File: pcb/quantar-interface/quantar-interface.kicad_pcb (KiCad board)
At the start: 4 copper layers, 127 x 101.6 mm, 179 parts, among them J1 DC Input, J2 USB_A, J3 USB_B, J4 GPIO, J5 Quantar Audio, J6 Ext. Alarm Contact, J7 Ext. TX Inhb., J8 Quantar, J9 5V Out, K1 G6S-2, Q1 DMP3056L-7, Q2 2N7002, Q3 2N7002, Q4 2N7002, Q5 2N7002, Q6 2N7002, SW1 SW_TX_INHB, SW2 SW_PTT_INHB, T1 Transformer, T2 Transformer, U1 M93C46, U10 4N27, U11 4N27, U12 4N27, U13 4N27, U14 4N27, U15 74HC14, U2 LM386, U3 TPS562200, U4 AP1506, U5 CM119A, U6 LM1117-5.0, U7 LM555, U8 4N27, U9 4N27, Y1 12MHz

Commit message: Add fiducials for PCBA
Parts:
- added REF1: Fiducial_1mm_Mask2mm, Fiducial:Fiducial_1mm_Mask2mm, F.Cu at (189.2, 62.2)
- added REF2: Fiducial_1mm_Mask2mm, Fiducial:Fiducial_1mm_Mask2mm, F.Cu at (81.3, 142.2)
- moved C15 76.2 mm to (168.1, 130.6)
- moved C17 76.2 mm to (134.1, 128.8)
- moved C25 76.2 mm to (134.1, 122.2)
- moved C27 76.2 mm to (117.9, 127.7)
- moved C32 76.2 mm to (107.5, 144.0)
- moved C33 76.2 mm to (119.4, 138.9)
- moved C7 76.2 mm to (150.4, 141.5)
- moved D10 76.2 mm to (140.5, 128.0)
- moved D13 76.2 mm to (134.9, 75.9)
- moved D19 76.2 mm to (130.3, 111.5)
- moved J7 76.2 mm to (153.7, 59.7)
- moved J9 76.2 mm to (99.7, 122.4)
- moved Q3 76.2 mm to (134.9, 80.3)
- moved R1 76.2 mm to (86.9, 124.2)
- moved R11 76.2 mm to (103.9, 105.4)
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
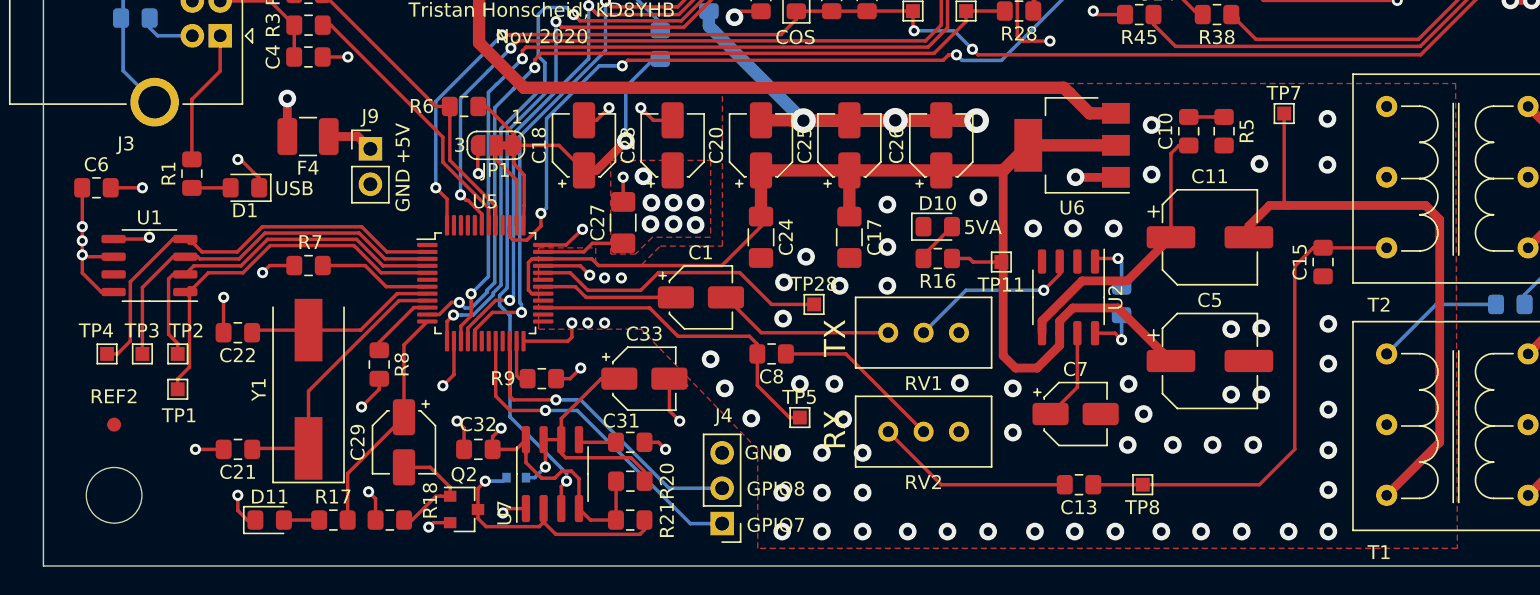
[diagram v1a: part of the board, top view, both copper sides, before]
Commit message: Add bottom layer plane to analog area
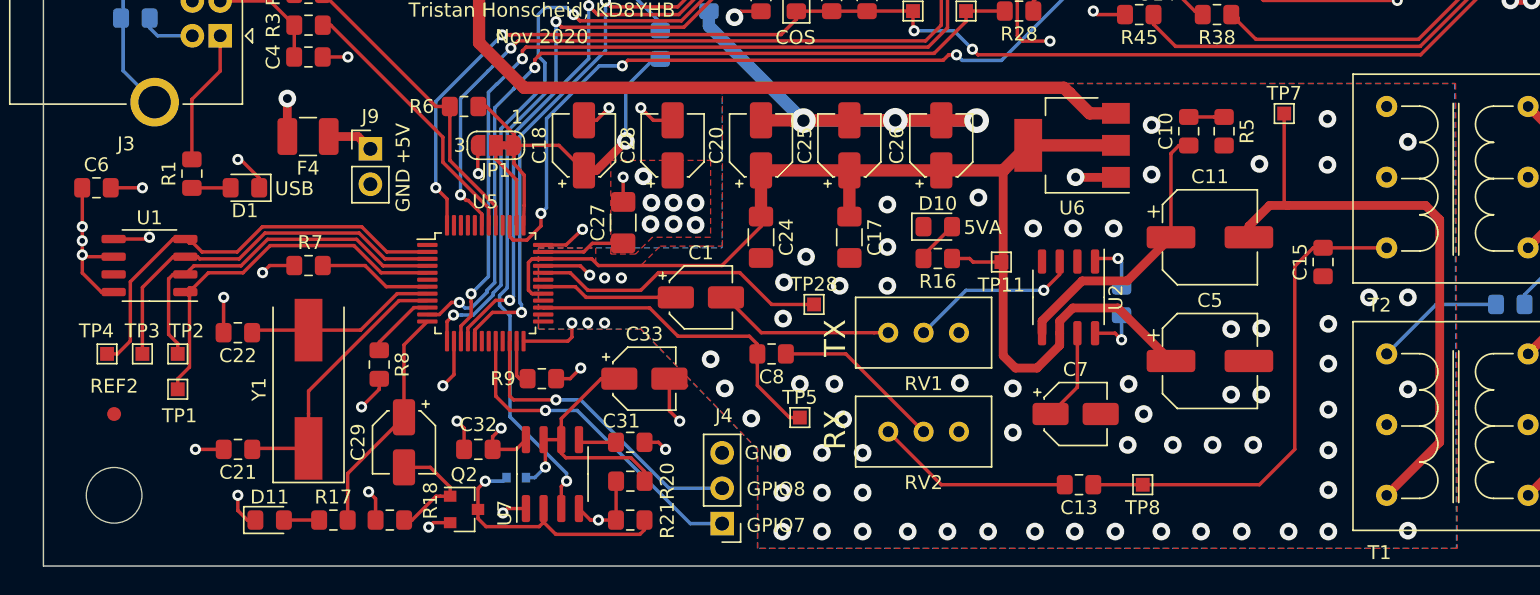
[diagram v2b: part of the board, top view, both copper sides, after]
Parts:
- moved REF2 0.76 mm to (81.3, 141.5)
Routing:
- net +5V: track 44.1 -> 35.6 mm, vias 23 -> 24
- net GNDA: vias 69 -> 74
- added copper zone on B.Cu, net GNDA
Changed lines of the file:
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@@
     (35 F.Paste user hide)
     (36 B.SilkS user)
-    (37 F.SilkS user)
+    (37 F.SilkS user hide)
     (38 B.Mask user)
-    (39 F.Mask user)
+    (39 F.Mask user hide)
     (40 Dwgs.User user)
     (41 Cmts.User user hide)
@@
     (43 Eco2.User user hide)
     (44 Edge.Cuts user)
-    (45 Margin user hide)
-    (46 B.CrtYd user hide)
-    (47 F.CrtYd user hide)
+    (45 Margin user)
+    (46 B.CrtYd user)
+    (47 F.CrtYd user)
     (48 B.Fab user hide)
     (49 F.Fab user hide)
@@
   )
   (module Fiducial:Fiducial_1mm_Mask2mm (layer F.Cu)
-    (at 81.28 142.24)
+    (at 81.28 141.478)
     (descr "Circular Fiducial, 1mm bare copper, 2mm soldermask opening (Level A)")
     (tags fiducial)
@@
   (segment (start 98.062 149.098) (end 98.062 145.756) (width 0.25) (layer F.Cu) (net 26))
   (segment (start 115.508 149.098) (end 114.681 148.271) (width 0.25) (layer F.Cu) (net 3))
-  (segment (start 117.339 149.098) (end 115.508 149.098) (width 0.25) (layer F.Cu) (net 3))
+  (segment (start 117.339 149.098) (end 116.078 149.098) (width 0.25) (layer F.Cu) (net 3))
   (segment (start 117.348 149.089) (end 117.339 149.098) (width 0.25) (layer F.Cu) (net 3))
   (segment (start 117.348 146.304) (end 117.348 149.089) (width 0.25) (layer F.Cu) (net 3))
-  (segment (start 114.681 148.271) (end 114.681 146.119998) (width 0.25) (layer F.Cu) (net 3))
-  (segment (start 114.681 146.119998) (end 114.140001 145.578999) (width 0.25) (layer F.Cu) (net 3))
-  (segment (start 113.443999 145.578999) (end 112.935999 146.086999) (width 0.25) (layer F.Cu) (net 3))
-  (segment (start 114.140001 145.578999) (end 113.443999 145.578999) (width 0.25) (layer F.Cu) (net 3))
-  (segment (start 110.871 144.296) (end 110.871 143.321) (width 0.25) (layer F.Cu) (net 3))
-  (segment (start 112.935999 146.086999) (end 111.993997 146.086999) (width 0.25) (layer F.Cu) (net 3))
-  (segment (start 111.993997 146.086999) (end 110.871 144.964002) (width 0.25) (layer F.Cu) (net 3))
-  (segment (start 110.871 144.964002) (end 110.871 144.296) (width 0.25) (layer F.Cu) (net 3))
   (via (at 86.614 86.6775) (size 1.778) (drill 0.889) (layers F.Cu B.Cu) (net 3))
   (via (at 86.6775 91.694) (size 1.778) (drill 0.889) (layers F.Cu B.Cu) (net 3))
@@
   (via (at 93.726 118.8085) (size 1.27) (drill 0.635) (layers F.Cu B.Cu) (net 3))
   (segment (start 93.726 121.539) (end 93.726 118.8085) (width 0.635) (layer F.Cu) (net 3))
+  (segment (start 115.824 149.098) (end 115.508 149.098) (width 0.25) (layer F.Cu) (net 3))
+  (segment (start 116.078 149.098) (end 115.824 149.098) (width 0.25) (layer F.Cu) (net 3))
+  (via (at 116.078 149.098) (size 0.8) (drill 0.4) (layers F.Cu B.Cu) (net 3))
   (segment (start 83.829 113.73) (end 83.829 113.03) (width 0.25) (layer B.Cu) (net 4))
   (segment (start 84.399 114.3) (end 83.829 113.73) (width 0.25) (layer B.Cu) (net 4))
@@
   (via (at 155.829 124.2695) (size 1.27) (drill 0.635) (layers F.Cu B.Cu) (net 8))
   (via (at 155.829 120.7135) (size 1.27) (drill 0.635) (layers F.Cu B.Cu) (net 8))
+  (via (at 171.45 133.096) (size 1.27) (drill 0.635) (layers F.Cu B.Cu) (net 8))
+  (via (at 174.244 133.096) (size 1.27) (drill 0.635) (layers F.Cu B.Cu) (net 8))
+  (via (at 174.244 139.7) (size 1.27) (drill 0.635) (layers F.Cu B.Cu) (net 8))
+  (via (at 174.244 149.86) (size 1.27) (drill 0.635) (layers F.Cu B.Cu) (net 8))
+  (via (at 174.244 121.92) (size 1.27) (drill 0.635) (layers F.Cu B.Cu) (net 8))
   (segment (start 150.495 139.551) (end 148.568 141.478) (width 0.25) (layer F.Cu) (net 9))
   (segment (start 150.495 135.671) (end 150.495 139.551) (width 0.25) (layer F.Cu) (net 9))
@@
       )
     )
+  )
+  (zone (net 8) (net_name GNDA) (layer B.Cu) (hatch edge 0.508)
+    (connect_pads yes (clearance 0.508))
+    (min_thickness 0.254)
+    (fill yes (arc_segments 32) (thermal_gap 0.508) (thermal_bridge_width 0.508))
+    (polygon
+      (pts
+        (xy 177.7365 151.13) (xy 127.508 151.13) (xy 127.508 144.018) (xy 119.126 135.382) (xy 111.76 135.382)
+        (xy 111.76 129.54) (xy 124.968 129.54) (xy 124.968 117.729) (xy 177.6095 117.729)
+      )
+    )

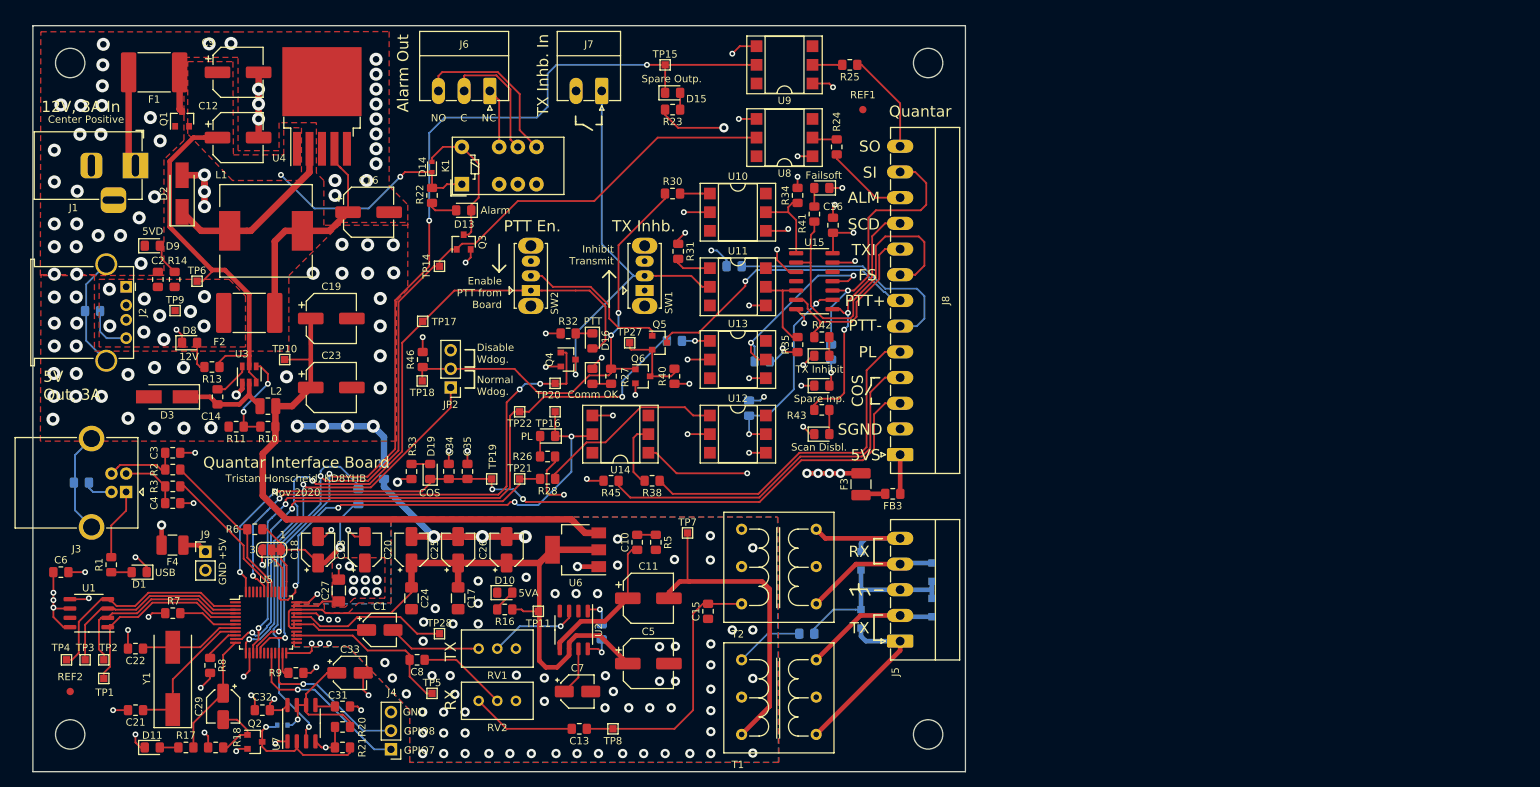
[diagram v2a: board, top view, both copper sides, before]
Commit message: Merge split ground planes, connect mounting holes to GND
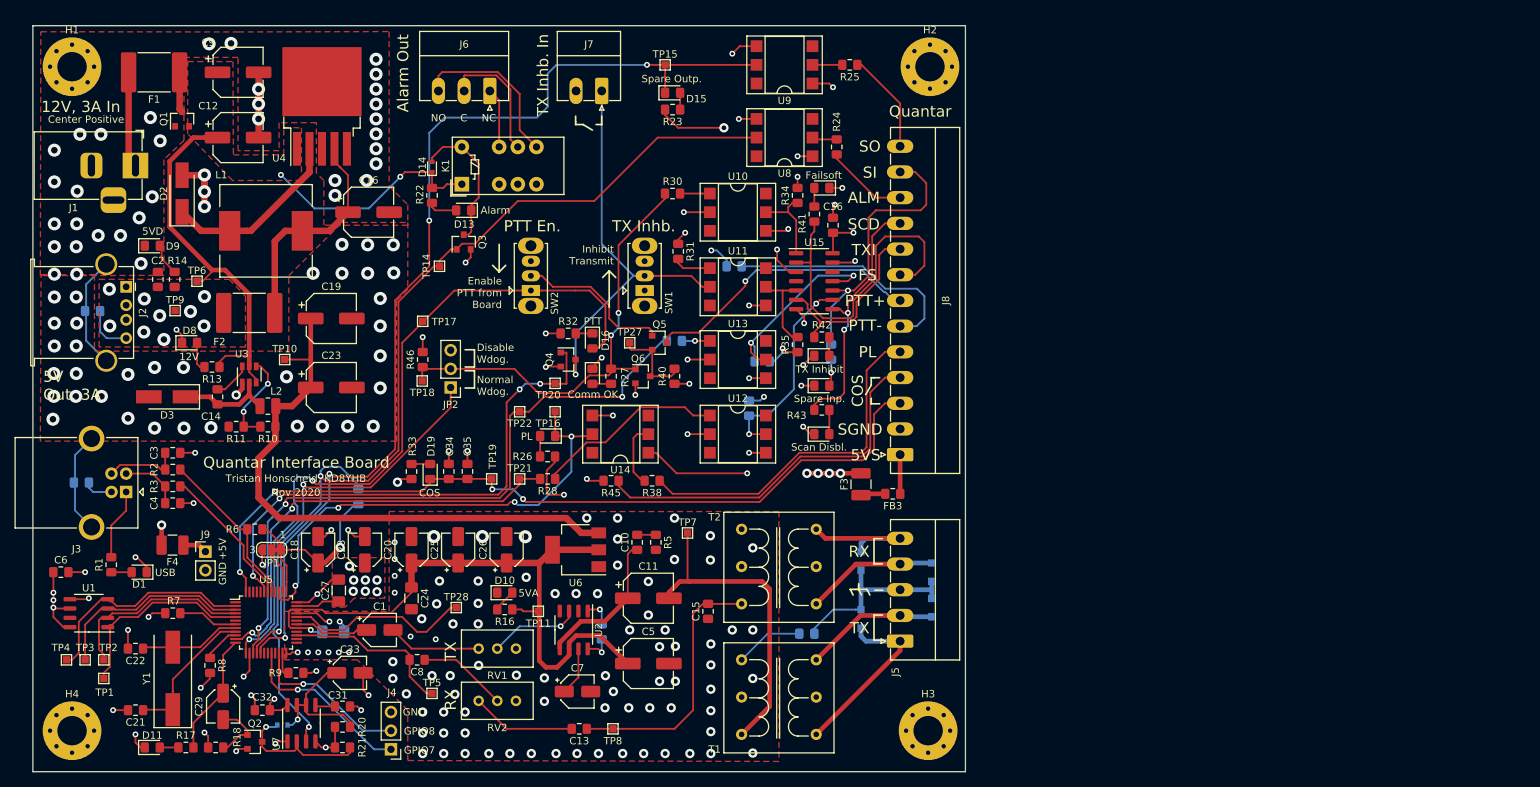
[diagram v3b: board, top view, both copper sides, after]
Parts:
- removed R15: 0, Resistor_SMD:R_0805_2012Metric_Pad1.15x1.40mm_HandSolder
- removed REF1, REF2: Fiducial_1mm_Mask2mm, Fiducial:Fiducial_1mm_Mask2mm
- C17: moved to B.Cu
- H1, H2, H3, H4: value MountingHole -> MountingHole_Pad; footprint MountingHole:MountingHole_4mm -> MountingHole:MountingHole_4mm_Pad_Via
- moved C17 17.6 mm to (117.1, 133.3), turned to 0 degrees
- moved TP28 4.23 mm to (133.9, 130.0)
- moved H1 0.57 mm to (81.5, 56.4)
- moved H2 0.57 mm to (198.4, 56.4)
- moved H4 0.57 mm to (81.5, 146.8)
- moved H3 0.51 mm to (198.1, 146.8)
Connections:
- C15 pad 2: GNDA -> GND
- C17 pad 2: GNDA -> GND
- C20 pad 2: GNDA -> GND
- C24 pad 2: GNDA -> GND
- C25 pad 2: GNDA -> GND
- C26 pad 2: GNDA -> GND
- C5 pad 2: GNDA -> Net-(C5-Pad2)
- C7 pad 2: GNDA -> Net-(C7-Pad2)
- D10 pad 1: GNDA -> GND
- H1 pad 1: (no net) -> GND
- H2 pad 1: (no net) -> GND
- H3 pad 1: (no net) -> GND
- H4 pad 1: (no net) -> GND
- R12 pad 2: GNDA -> GND
- R5 pad 2: GNDA -> GND
- RV1 pad 3: GNDA -> GND
- RV2 pad 3: GNDA -> GND
- T1 pad 1: GNDA -> GND
- T2 pad 1: GNDA -> GND
- U2 pad 2: GNDA -> GND
- U2 pad 4: GNDA -> GND
- U5 pad 24: GNDA -> GND
- U5 pad 33: GNDA -> GND
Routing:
- net GNDA: track 56.2 -> 0.00 mm, vias 74 -> 0
- net GND: track 153.3 -> 165.9 mm, vias 120 -> 202
- net /LINEOUT_RIGHT: track 21.5 -> 25.4 mm
- net Net-(C19-Pad1): track 79.6 -> 80.6 mm
- net +5VA: track 88.7 -> 89.1 mm, vias 0 -> 1
- removed copper zone on B.Cu, net GNDA
- removed copper zone on F.Cu, net GNDA
- removed copper zone on In2.Cu, net GNDA

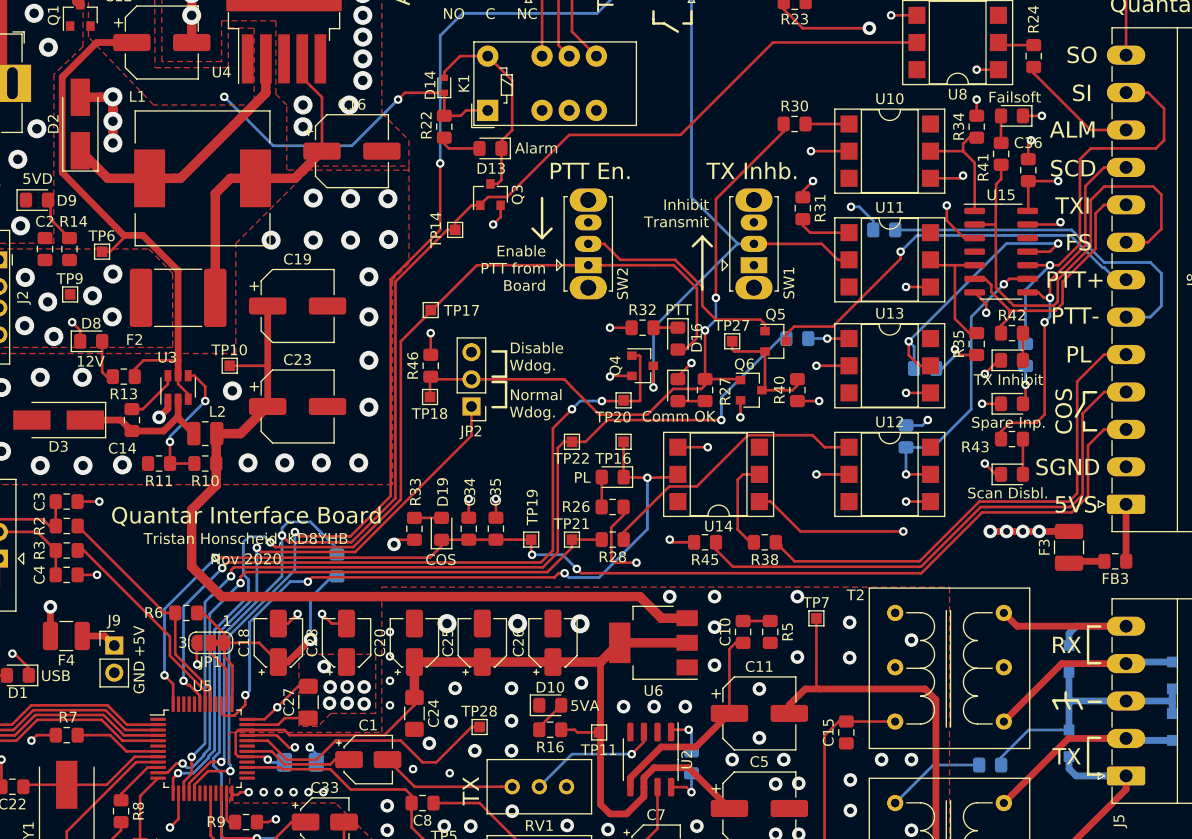
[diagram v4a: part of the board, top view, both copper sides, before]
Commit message: Plot gerbers, generate JLCPCB BOM and picklist, move all JLC components to top side
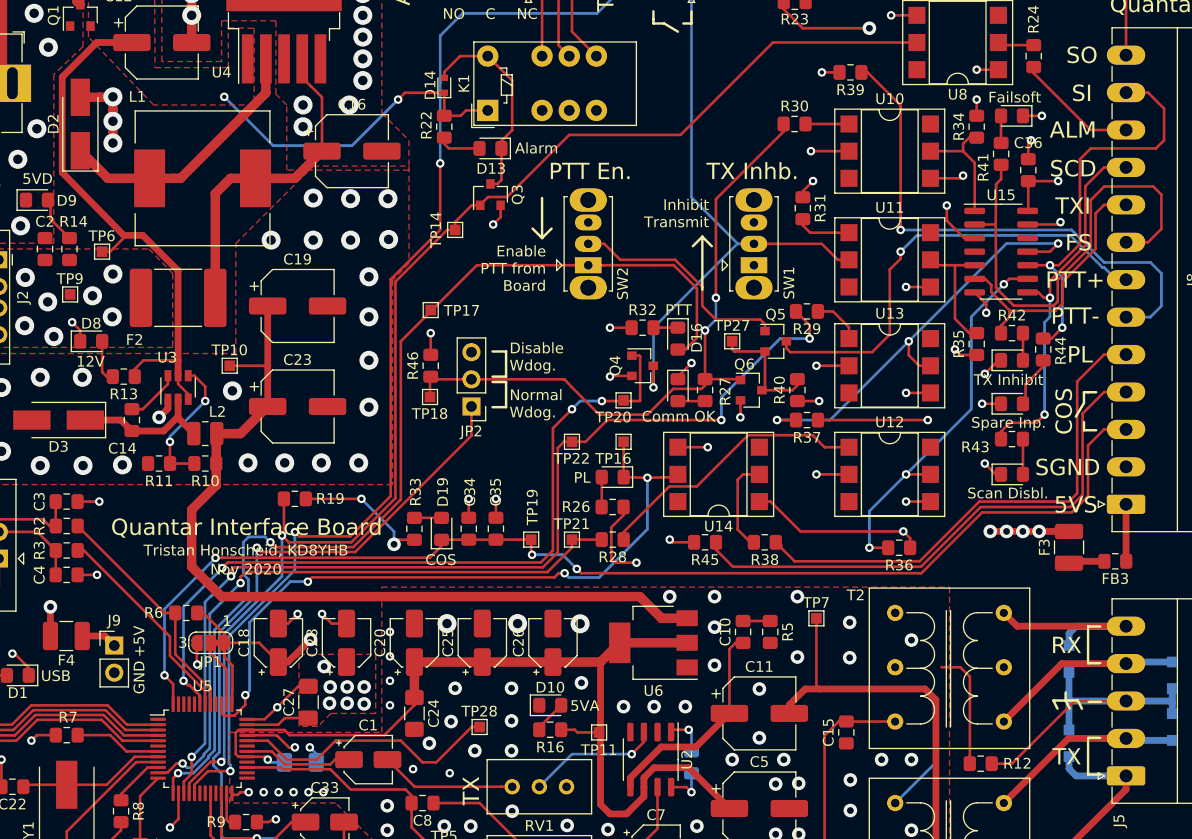
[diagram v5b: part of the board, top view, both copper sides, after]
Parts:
- R12, R19, R29, R36, R37, R39, R44: moved to F.Cu
- moved R39 15.1 mm to (168.5, 68.8)
- moved R37 12.0 mm to (164.5, 101.3)
- moved R36 10.4 mm to (173.1, 113.3), turned to 180 degrees
- moved R19 7.36 mm to (116.6, 108.7), turned to 180 degrees
- moved R29 2.69 mm to (164.5, 91.2)
- moved R44 1.73 mm to (186.6, 94.7)
- moved R12 0.89 mm to (180.7, 133.5)
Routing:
- net /STATION_PTT_LED+: track 33.4 -> 49.4 mm, vias 0 -> 1
- net Net-(R37-Pad2): track 27.4 -> 41.8 mm, vias 2 -> 3
- net Net-(R36-Pad2): track 27.8 -> 36.3 mm, vias 2 -> 3
- net /STATION_5V: track 41.5 -> 48.4 mm
- net Net-(D4-Pad2): track 25.5 -> 32.4 mm
- net GND: track 165.9 -> 172.7 mm
- net /SPARE_INPUT: track 90.6 -> 95.8 mm, vias 3 -> 4
- net /STATION_PTT_LED-: track 38.4 -> 42.8 mm
- net /ALARM: track 127.3 -> 123.1 mm
- net +5V: track 35.6 -> 33.8 mm
- net +3V3: track 159.9 -> 161.2 mm, vias 4 -> 5
- net Net-(D23-Pad2): track 3.65 -> 4.84 mm, vias 1 -> 0
- net Net-(R29-Pad1): track 3.81 -> 4.58 mm, vias 1 -> 0
- net /STATION_SPARE_INPUT: track 37.7 -> 37.9 mm, vias 1 -> 2

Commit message: Revision B
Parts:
- added R15: 100K, Resistor_SMD:R_0805_2012Metric_Pad1.15x1.40mm_HandSolder, F.Cu at (151.4, 88.5)
- added SW3: Force PTT, Button_Switch_SMD:SW_Push_1P1T_NO_CK_KMR2, F.Cu at (156.1, 70.1)
- moved C6 8.62 mm to (78.6, 133.7), turned to 270 degrees
- moved F4 1.23 mm to (94.0, 121.5)
- moved J5 0.76 mm to (195.1, 134.6)
- moved J6 0.76 mm to (138.4, 58.9)
- moved J7 0.76 mm to (153.7, 58.9)
- moved J8 0.76 mm to (195.1, 109.2)
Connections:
- C5 pad 2: Net-(C5-Pad2) -> GND
- C7 pad 2: Net-(C7-Pad2) -> GND
- D16 pad 1: Net-(D16-Pad1) -> /STATION_PTT_LED-
- D16 pad 2: /PTT -> Net-(D16-Pad2)
- R32 pad 1: GND -> +5V
- R32 pad 2: Net-(D16-Pad1) -> Net-(D16-Pad2)
- SW2 pad 3: GND -> Net-(SW2-Pad3)
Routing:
- net /STATION_PTT_LED-: track 42.8 -> 83.6 mm, vias 1 -> 3
- net /PTT: track 97.8 -> 79.9 mm
- net GND: track 172.7 -> 177.7 mm, vias 202 -> 204
- net /ALARM: track 123.1 -> 127.5 mm
- net Net-(D16-Pad2): track 0.00 -> 3.39 mm
- net Net-(J6-Pad2): track 17.4 -> 20.4 mm
- net Net-(D16-Pad1): track 2.29 -> 0.00 mm
- net Net-(J6-Pad3): track 22.7 -> 25.0 mm
- net /STATION_PTT_LED+: track 49.4 -> 51.3 mm
- net /STATION_SPARE_INPUT: track 37.9 -> 39.6 mm
- net /STATION_FAILSOFT: track 45.5 -> 47.3 mm
- net Net-(J6-Pad1): track 8.15 -> 9.74 mm
- net /RX_AUDIO_LINE2-: track 18.7 -> 20.2 mm
- net /TX_AUDIO_LINE1+: track 24.2 -> 25.5 mm
- net Net-(F4-Pad1): track 3.36 -> 4.60 mm
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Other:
- board text added: "Ctrl On"
- board text added: "Force PTT"
- board text added: "REV B"
- board text removed: "Failsoft"
